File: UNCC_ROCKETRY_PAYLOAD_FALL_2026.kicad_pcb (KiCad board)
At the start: 2 copper layers, 103 parts, among them J1 STDC14, J2 XT30PW-M, J3 ARM_SW, J4 CAMERA, J5 USB_C, Q1 AO3401A, Q2 AO3400A, SW1 BOOT0, U1 STM32F405RGTx, U10 W25Q512JVFIQ, U11 E22-900M30S, U12 TPS22917DBV, U13 MMC5983MA, U2 TPS54302, U3 AP2112K-3.3, U4 LSM6DSO32, U5 H3LIS331DLTR, U6 MS5611-01BA, U7 USBLC6-2SC6, U8 SHT45-AD1F-R2, U9 SAM-M10Q-00B, Y1 8MHz

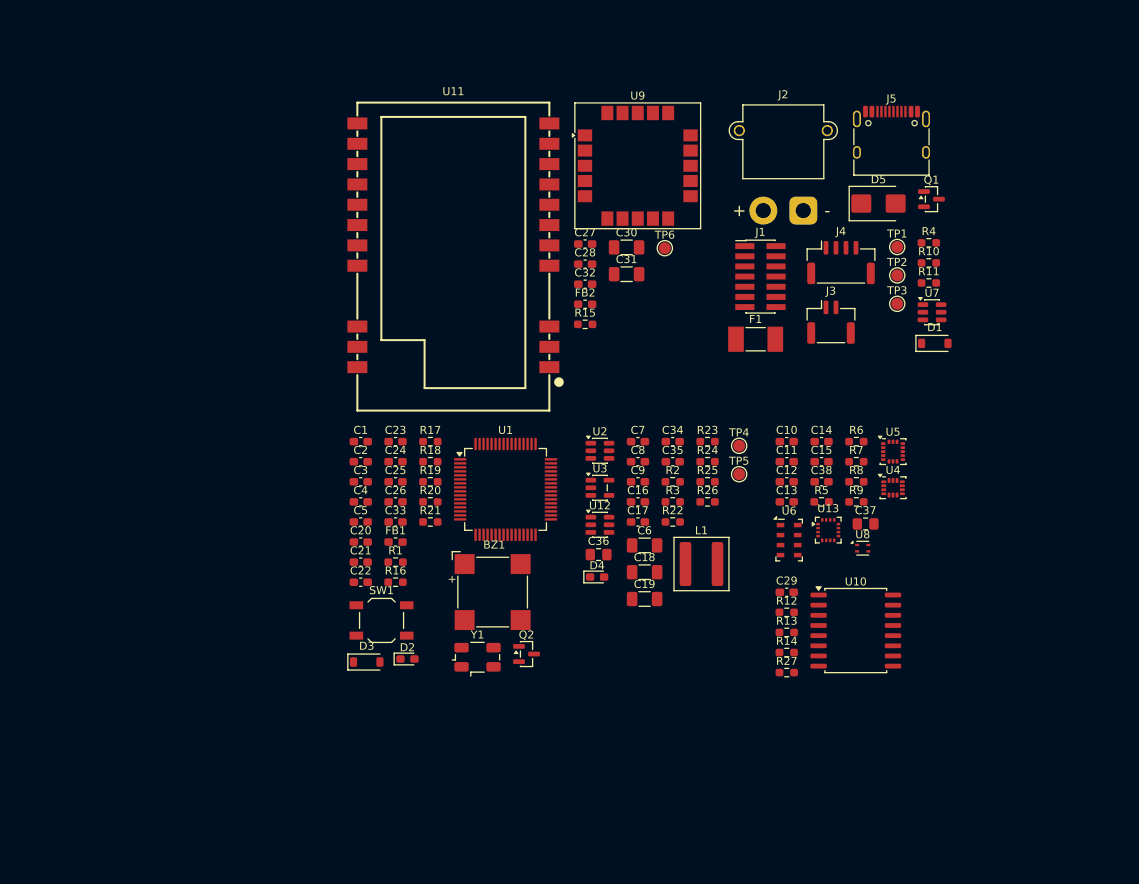
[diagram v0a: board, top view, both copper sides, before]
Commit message: layed out components, no routing
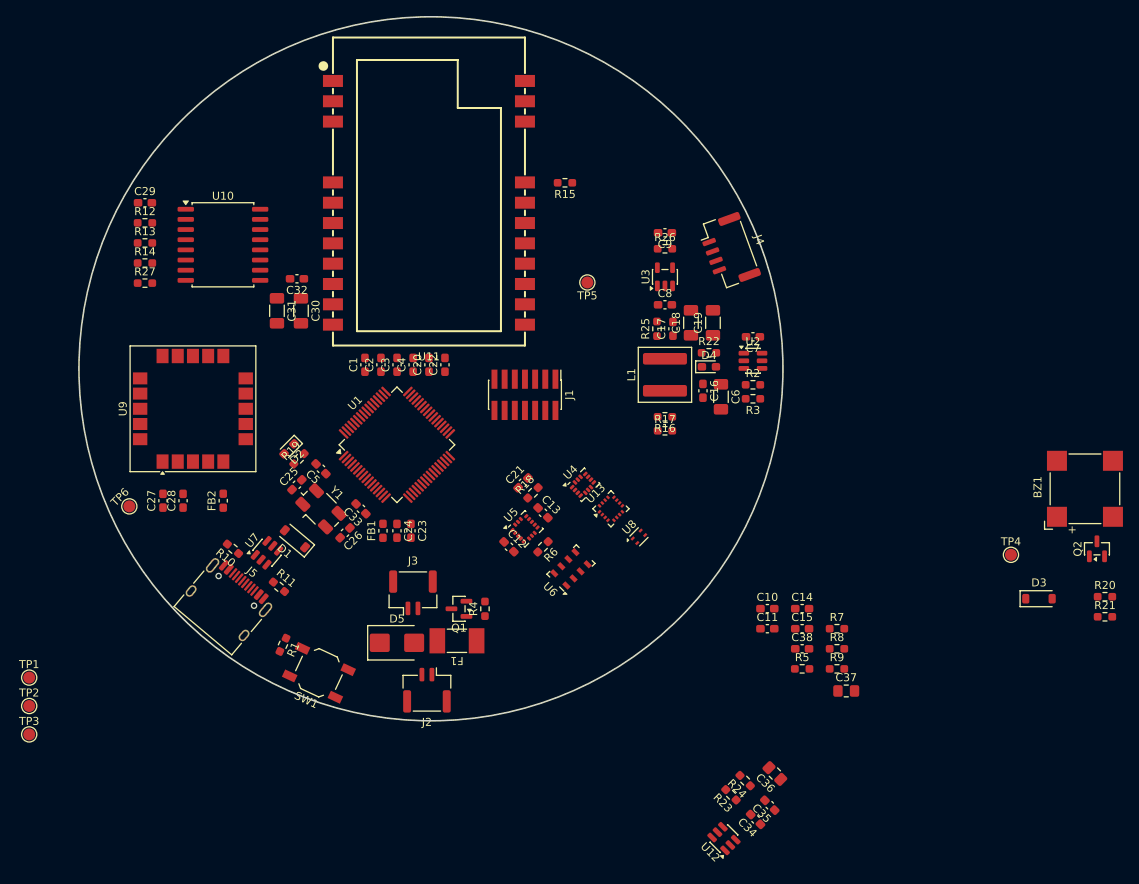
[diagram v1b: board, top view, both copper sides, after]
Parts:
- J2: footprint Connector_AMASS:AMASS_XT30PW-M_1x02_P2.50mm_Horizontal -> Connector_JST:JST_GH_BM02B-GHS-TBT_1x02-1MP_P1.25mm_Vertical
- J3: footprint Connector_JST:JST_GH_SM02B-GHS-TB_1x02-1MP_P1.25mm_Horizontal -> Connector_JST:JST_GH_BM02B-GHS-TBT_1x02-1MP_P1.25mm_Vertical
- J4: footprint Connector_JST:JST_GH_SM04B-GHS-TB_1x04-1MP_P1.25mm_Horizontal -> Connector_JST:JST_GH_BM04B-GHS-TBT_1x04-1MP_P1.25mm_Vertical
- moved TP2 121.1 mm to (74.8, 142.2)
- moved TP1 121.1 mm to (74.8, 138.6)
- moved TP3 121.1 mm to (74.8, 145.7)
- moved J5 101.6 mm to (99.0, 129.8), turned to -40 degrees
- moved R10 94.0 mm to (100.2, 122.5), turned to 140 degrees
- moved C29 93.8 mm to (89.2, 79.2)
- moved R13 93.8 mm to (89.2, 84.3)
- moved R14 93.8 mm to (89.2, 86.8)
- moved R12 93.8 mm to (89.2, 81.8)
- moved R27 93.8 mm to (89.2, 89.3)
- moved U10 92.6 mm to (99.0, 84.5)
- moved R11 89.7 mm to (106.0, 127.2), turned to -40 degrees
- moved U7 88.4 mm to (104.5, 123.0), turned to 50 degrees
- moved R20 85.2 mm to (209.2, 128.5)
- moved R21 85.2 mm to (209.2, 131.0)
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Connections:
- R15 pad 2: /RF/LORA_CS -> /MCU/LORA_CS
- U11 pad 13: /RF/LORA_DIO1 -> /MCU/LORA_DIO1
- U11 pad 14: /RF/LORA_BUSY -> /MCU/LORA_BUSY
- U11 pad 15: /RF/LORA_NRST -> /MCU/LORA_NRST
- U11 pad 16: /RF/LORA_MISO -> /MCU/LORA_MISO
- U11 pad 17: /RF/LORA_MOSI -> /MCU/LORA_MOSI
- U11 pad 18: /RF/LORA_SCK -> /MCU/LORA_SCK
- U11 pad 19: /RF/LORA_CS -> /MCU/LORA_CS
- U11 pad 6: /RF/LORA_RXEN -> /MCU/LORA_RXEN
- U9 pad 13: /RF/TX_GPS -> /MCU/TX_GPS
- U9 pad 14: /RF/RX_GPS -> /MCU/RX_GPS
- U9 pad 18: /RF/RESET_GPS -> /MCU/RESET_GPS
- U9 pad 7: /RF/TIMER_GPS -> /MCU/TIMER_GPS
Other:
- board outline added: 88 x 88 mm
